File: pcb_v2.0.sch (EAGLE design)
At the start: 39 parts, among them J1 PJ301_THONKICONN6, J2 PJ301_THONKICONN6, J3 PJ301_THONKICONN6, J4 PJ301_THONKICONN6, U1 MCP6004, U5 TL074

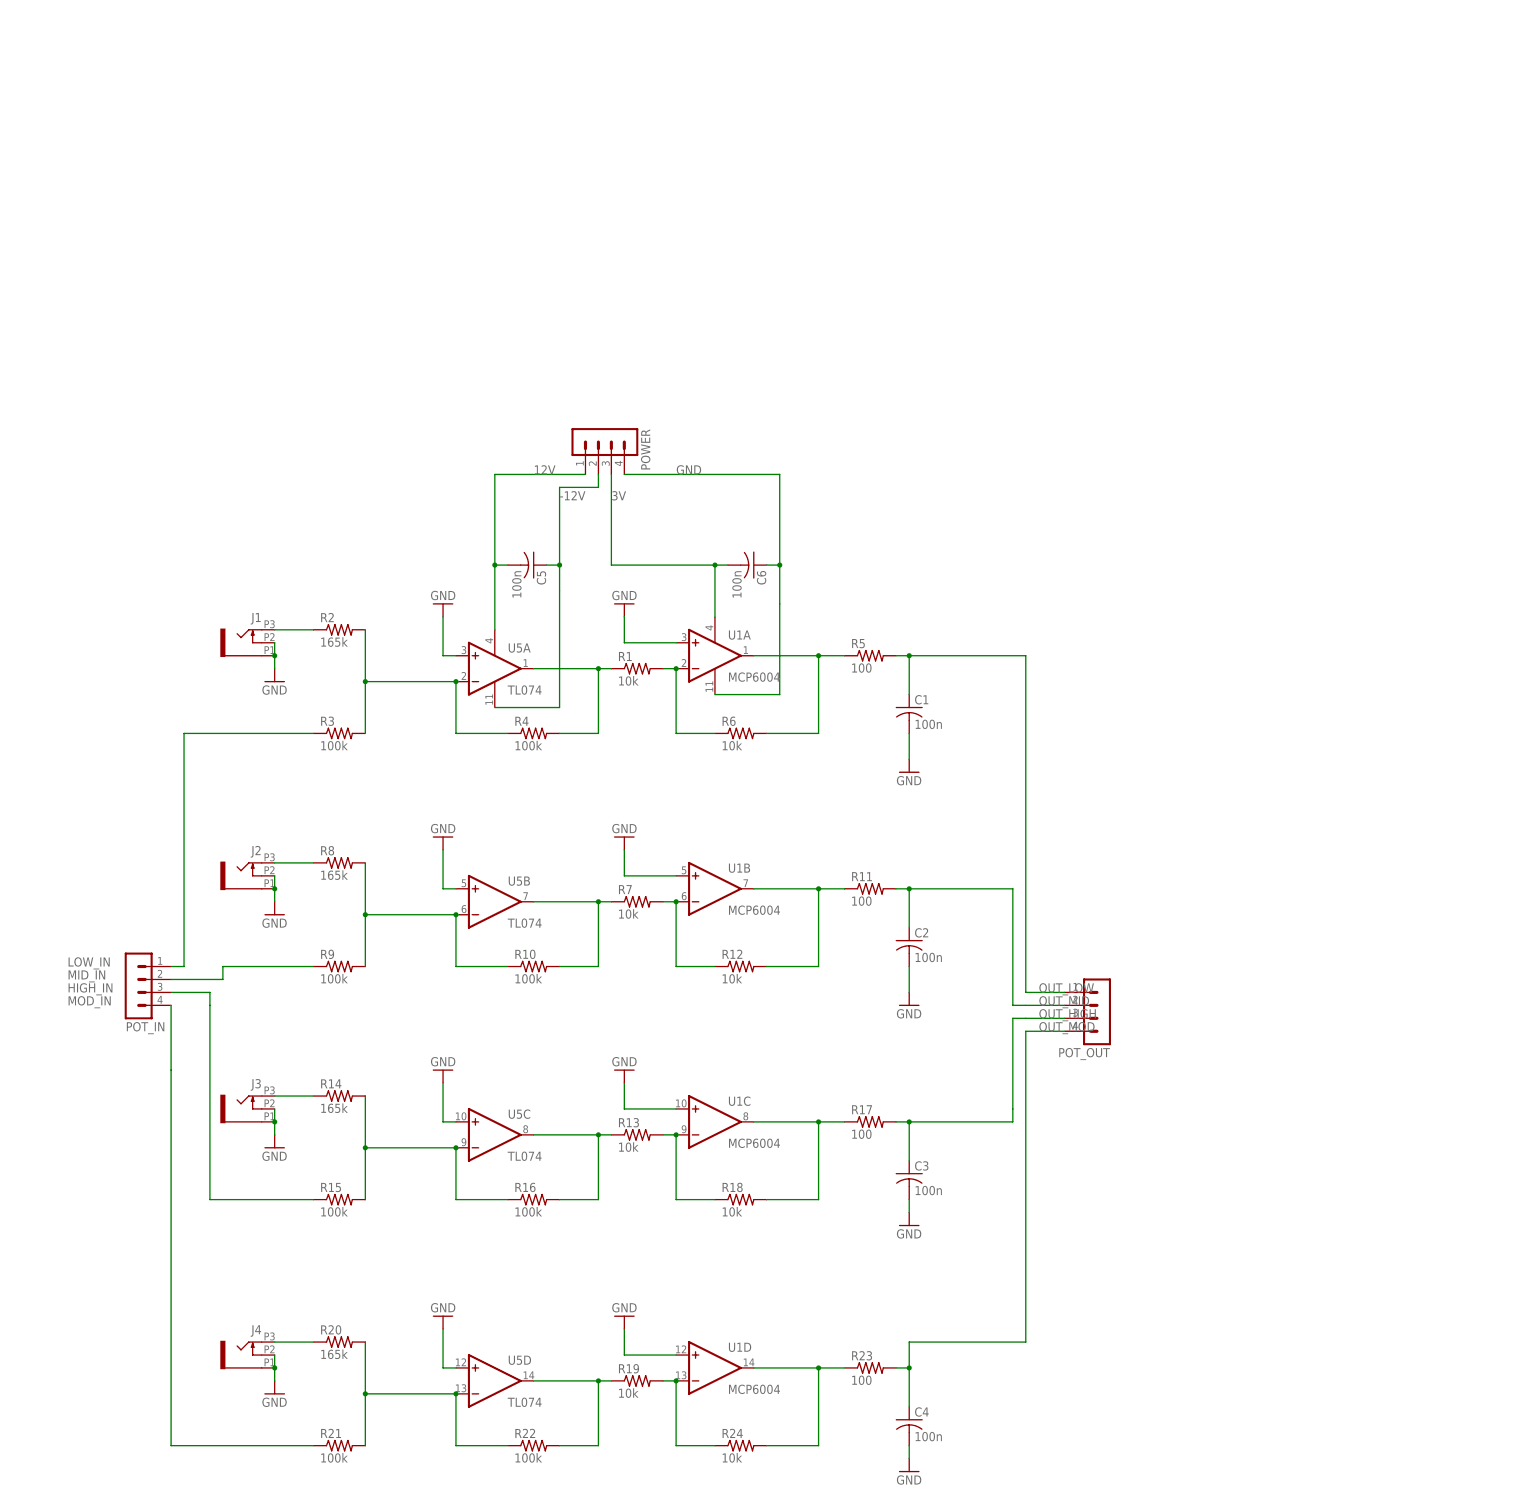
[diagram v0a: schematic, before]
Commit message: create base schematic for sd card and attenuators
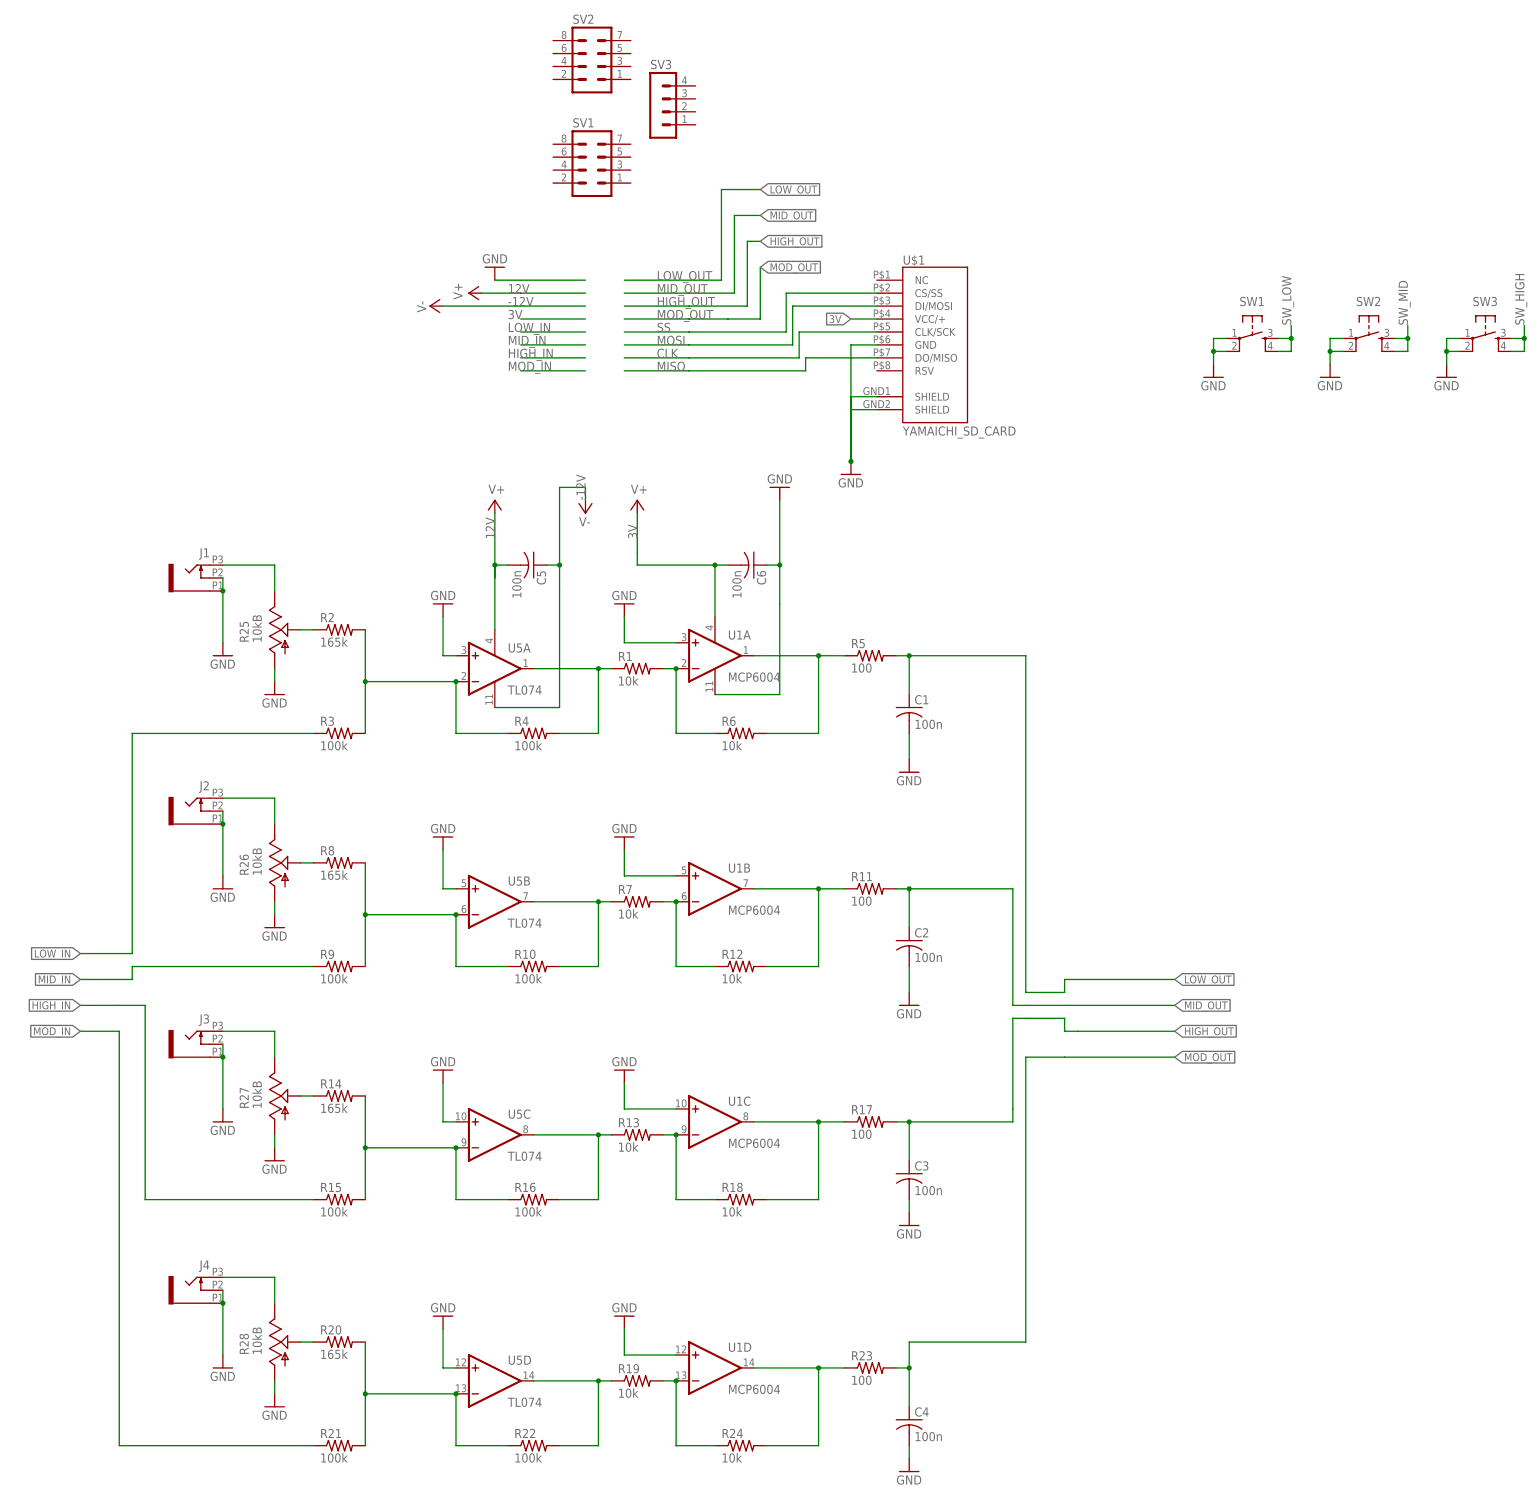
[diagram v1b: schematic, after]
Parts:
- removed POT_IN, POT_OUT, POWER: (no value), con-lstb:MA04-1
- added R25, R26, R27, R28: 10kB, og-pots:POT_USVERTICAL
- added SV1, SV2: (no value), con-lstb:MA04-2
- added SV3: (no value), con-lstb:MA04-1
- added SW1, SW2, SW3: (no value), SparkFun:TAC_SWITCHPTH
- added U$1: YAMAICHI_SD_CARD, MusicThingModular:YAMAICHI_SD_CARD
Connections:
- removed net OUT_HIGH: C3.1, POT_OUT.3, R17.2
- removed net OUT_LOW: C1.1, POT_OUT.1, R5.2
- removed net OUT_MID: C2.1, POT_OUT.2, R11.2
- removed net OUT_MOD: C4.1, POT_OUT.4, R23.2
- new net CLK: U$1.CLK/SCK
- new net HIGH_OUT: C3.1, R17.2
- new net LOW_OUT: C1.1, R5.2
- new net MID_OUT: C2.1, R11.2
- new net MISO: U$1.DO/MISO
- new net MOD_OUT: C4.1, R23.2
- new net MOSI: U$1.DI/MOSI
- new net N$10: R2.1, R25.S
- new net N$12: R14.1, R27.S
- new net N$15: R20.1, R28.S
- new net N$2: J2.3, R26.E
- new net N$7: J4.3, R28.E
- new net SS: U$1.CS/SS
- new net SW_HIGH: SW3.3, SW3.4
- new net SW_LOW: SW1.3, SW1.4
- new net SW_MID: SW2.3, SW2.4
- net -12V: no longer POWER.2
- net 12V: no longer POWER.1
- net 3V: no longer POWER.3
- net GND: now also R25.A, R26.A, R27.A, R28.A, SW1.1, SW1.2, SW2.1, SW2.2, SW3.1, SW3.2, U$1.GND, U$1.SHIELD@1, U$1.SHIELD@2; no longer POWER.4
- net HIGH_IN: no longer POT_IN.3
- net LOW_IN: no longer POT_IN.1
- net MID_IN: no longer POT_IN.2
- net MOD_IN: no longer POT_IN.4
- net N$1: now also R25.E; no longer R2.1
- net N$11: now also R26.S, R8.1; no longer J3.3, R14.1
- net N$16: now also U$1.VCC/+; no longer J4.3, R20.1
- net N$6: now also J3.3, R27.E; no longer J2.3, R8.1
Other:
- moved on the sheet: J1, J2, J3, J4
